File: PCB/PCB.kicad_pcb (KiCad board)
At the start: 2 copper layers, 22.8 x 29.9 mm, 5 parts

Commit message: feat: add components
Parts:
- added U1: STM32G031F6P6, Package_SO:TSSOP-20_4.4x6.5mm_P0.65mm, F.Cu at (157.9, 69.3)
- added U2: XN297L, Package_SO:SSOP-16_3.9x4.9mm_P0.635mm, F.Cu at (165.5, 75.5)
- added U3: HT7333-3.3V, Package_TO_SOT_SMD:SOT-89-3, F.Cu at (165.5, 68.5)
- GND1, SN1, SN2, SN3, VCC1: footprint TestPoint:TestPoint_THTPad_2.0x2.0mm_Drill1.0mm -> TestPoint:TestPoint_THTPad_1.0x1.0mm_Drill0.5mm
- moved GND1 5.41 mm to (155.0, 83.5)
- moved SN3 5.41 mm to (167.0, 83.5)
- moved SN2 4.74 mm to (164.0, 83.5)
- moved VCC1 4.74 mm to (158.0, 83.5)
- moved SN1 4.50 mm to (161.0, 83.5)
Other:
- board size 22.8 x 29.9 mm -> 15 x 20 mm
- board text added: "Nano2A - By Abstractmelon"
- board text removed: "By Abstractmelon"
- board text removed: "Nano2A"

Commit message: feat: added all components
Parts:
- added C1: C, Capacitor_SMD:C_0402_1005Metric, F.Cu at (162.0, 74.0)
- added C2: C, Capacitor_SMD:C_0402_1005Metric, F.Cu at (160.5, 76.0)
- added C3: C, Capacitor_SMD:C_0402_1005Metric, F.Cu at (162.0, 76.0)
- added C4: C, Capacitor_SMD:C_0402_1005Metric, F.Cu at (154.5, 78.0)
- added C5: C, Capacitor_SMD:C_0402_1005Metric, F.Cu at (156.5, 78.0)
- added C6: C, Capacitor_SMD:C_0402_1005Metric, F.Cu at (158.4, 78.0)
- added C7: C, Capacitor_SMD:C_0603_1608Metric, F.Cu at (159.5, 74.0)
- added L1: L, Inductor_SMD:L_0402_1005Metric, F.Cu at (158.9, 76.2)
- added Y1: Crystal, Crystal:Crystal_SMD_3225-4Pin_3.2x2.5mm, F.Cu at (155.9, 74.8)
- moved U2 1.13 mm to (165.5, 74.4)
- moved U3 1.12 mm to (166.0, 67.5)

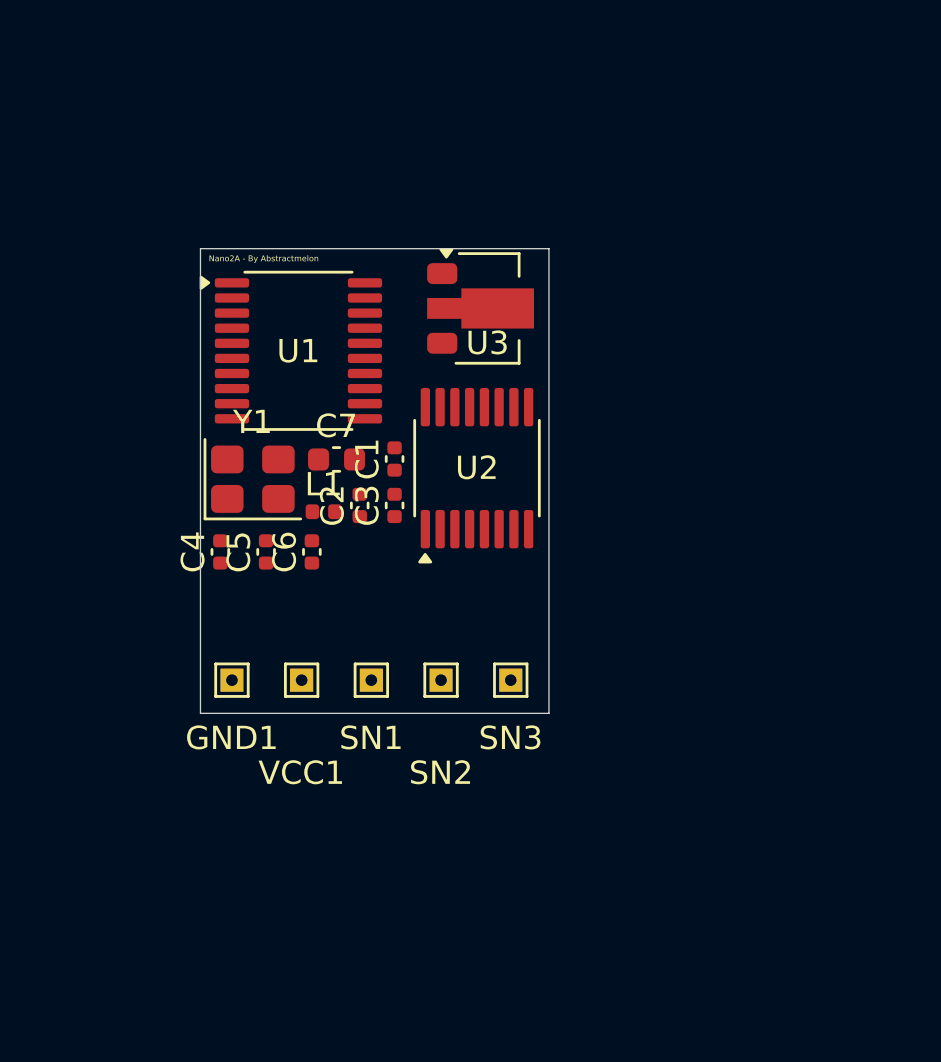
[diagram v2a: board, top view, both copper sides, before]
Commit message: feat: update PCB traces and move components
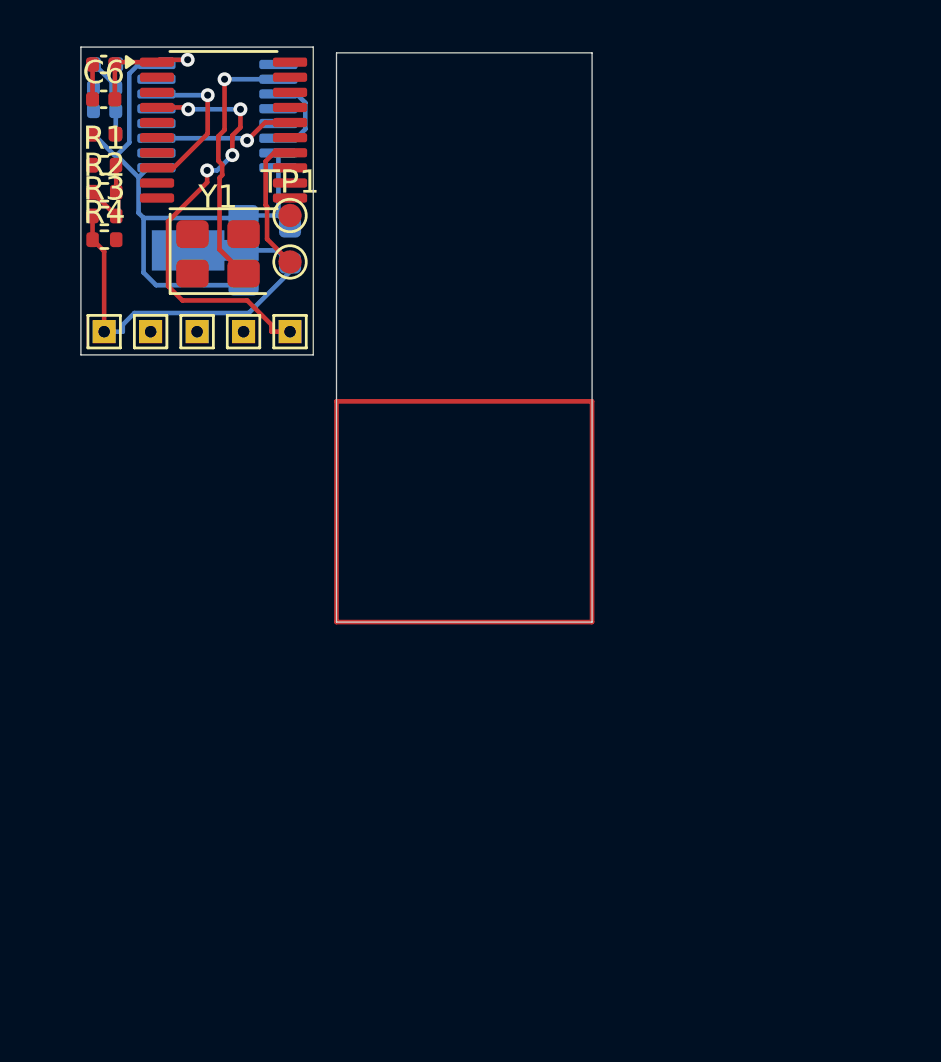
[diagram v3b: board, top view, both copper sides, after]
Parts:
- removed SN1: Channel 1, TestPoint:TestPoint_THTPad_1.0x1.0mm_Drill0.5mm
- removed SN2: Channel 2, TestPoint:TestPoint_THTPad_1.0x1.0mm_Drill0.5mm
- removed SN3: Channel 3, TestPoint:TestPoint_THTPad_1.0x1.0mm_Drill0.5mm
- added CH1: Channel 1, TestPoint:TestPoint_THTPad_1.0x1.0mm_Drill0.5mm, F.Cu at (153.5, 68.5)
- added CH2: Channel 2, TestPoint:TestPoint_THTPad_1.0x1.0mm_Drill0.5mm, F.Cu at (155.5, 68.5)
- added CH3: Channel 3, TestPoint:TestPoint_THTPad_1.0x1.0mm_Drill0.5mm, F.Cu at (157.5, 68.5)
- added R1: R, Resistor_SMD:R_0402_1005Metric, F.Cu at (149.5, 61.3)
- added R2: R, Resistor_SMD:R_0402_1005Metric, F.Cu at (149.5, 62.5)
- added R3: R, Resistor_SMD:R_0402_1005Metric, F.Cu at (149.5, 63.5)
- added R4: R, Resistor_SMD:R_0402_1005Metric, F.Cu at (149.5, 64.5)
- added TP1: SWDIO, TestPoint:TestPoint_Pad_D1.0mm, F.Cu at (157.5, 63.5)
- added TP2: SWCLK, TestPoint:TestPoint_Pad_D1.0mm, F.Cu at (157.5, 65.5)
- C1, C2, C3, C4, C7, U2, U3: moved to B.Cu
- moved C5 22.1 mm to (149.5, 57.0), turned to 0 degrees
- moved C3 21.9 mm to (149.5, 58.0), turned to 180 degrees
- moved C6 21.4 mm to (149.5, 58.5), turned to 0 degrees
- moved C1 21.0 mm to (149.6, 57.0), turned to 0 degrees
- moved C2 20.2 mm to (149.5, 59.0), turned to 180 degrees
- moved U2 18.8 mm to (154.4, 59.2), turned to 0 degrees
- moved L1 18.8 mm to (149.5, 60.0)
- moved C4 18.7 mm to (149.5, 60.0), turned to 180 degrees
- moved VCC1 16.3 mm to (151.5, 68.5), turned to 0 degrees
- moved GND1 16.0 mm to (149.5, 68.5), turned to 0 degrees
- moved U3 12.7 mm to (153.6, 65.0), turned to 180 degrees
- moved U1 10.0 mm to (154.6, 59.8)
- moved Y1 9.82 mm to (154.4, 65.2)
- moved C7 9.44 mm to (157.5, 64.8), turned to 90 degrees
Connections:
- C1 pad 1: unconnected-(C1-Pad1) -> /GND
- C1 pad 2: unconnected-(C1-Pad2) -> /ANT
- C2 pad 1: unconnected-(C2-Pad1) -> /GND
- C2 pad 2: unconnected-(C2-Pad2) -> /XC1
- C3 pad 1: unconnected-(C3-Pad1) -> /GND
- C3 pad 2: unconnected-(C3-Pad2) -> /XC2
- C4 pad 1: unconnected-(C4-Pad1) -> /GND
- C4 pad 2: unconnected-(C4-Pad2) -> /+3.3V
- C5 pad 1: unconnected-(C5-Pad1) -> /GND
- C5 pad 2: unconnected-(C5-Pad2) -> /+3.3V
- C6 pad 1: unconnected-(C6-Pad1) -> /GND
- C6 pad 2: unconnected-(C6-Pad2) -> /+3.3V
- C7 pad 1: unconnected-(C7-Pad1) -> /GND
- C7 pad 2: unconnected-(C7-Pad2) -> /+3.3V
- GND1 pad 1: unconnected-(GND1-Pad1) -> /GND
- L1 pad 2: unconnected-(L1-Pad2) -> /ANT
- U1 pad 1: unconnected-(U1-VDD-Pad1) -> /+3.3V
- U1 pad 14: unconnected-(U1-PA14-Pad14) -> /SWCLK
- U1 pad 15: unconnected-(U1-NRST-Pad15) -> /NRST
- U1 pad 16: unconnected-(U1-PB0-Pad16) -> /CSN
- U1 pad 2: unconnected-(U1-PA0-Pad2) -> /ADC
- U1 pad 3: unconnected-(U1-PA1-Pad3) -> /CH2
- U1 pad 4: unconnected-(U1-PA2-Pad4) -> /CH3
- U1 pad 5: unconnected-(U1-PA3-Pad5) -> /CE
- U1 pad 6: unconnected-(U1-PA4-Pad6) -> /IRQ
- U1 pad 7: unconnected-(U1-PA5-Pad7) -> /SCK
- U1 pad 8: unconnected-(U1-PA6-Pad8) -> /MISO
- U1 pad 9: unconnected-(U1-PA7-Pad9) -> /MOSI
- U2 pad 1: unconnected-(U2-VCC-Pad1) -> /+3.3V
- U2 pad 10: unconnected-(U2-XC2-Pad10) -> /XC2
- U2 pad 11: unconnected-(U2-VSS-Pad11) -> /GND
- U2 pad 12: unconnected-(U2-ANT-Pad12) -> /ANT
- U2 pad 13: unconnected-(U2-IREF-Pad13) -> /IREF
- U2 pad 14: unconnected-(U2-VSS_PA-Pad14) -> /GND
- U2 pad 15: unconnected-(U2-VDD_PA-Pad15) -> /+3.3V
- U2 pad 16: unconnected-(U2-VCC_PA-Pad16) -> /+3.3V
- U2 pad 2: unconnected-(U2-CE-Pad2) -> /CE
- U2 pad 3: unconnected-(U2-CSN-Pad3) -> /CSN
- U2 pad 4: unconnected-(U2-SCK-Pad4) -> /SCK
- U2 pad 5: unconnected-(U2-MOSI-Pad5) -> /MOSI
- U2 pad 6: unconnected-(U2-MISO-Pad6) -> /MISO
- U2 pad 7: unconnected-(U2-IRQ-Pad7) -> /IRQ
- U2 pad 8: unconnected-(U2-VDD-Pad8) -> /+3.3V
- U2 pad 9: unconnected-(U2-XC1-Pad9) -> /XC1
- U3 pad 1: unconnected-(U3-VIN-Pad1) -> /+3.3V
- U3 pad 2: unconnected-(U3-GND-Pad2) -> /GND
- U3 pad 3: unconnected-(U3-VOUT-Pad3) -> /+3.3V
- Y1 pad 1: unconnected-(Y1-Pad1) -> /XC1
- Y1 pad 2: unconnected-(Y1-Pad2) -> /XC2
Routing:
- net /+3.3V: track 0.00 -> 34.0 mm, vias 0 -> 1
- net /GND: track 0.00 -> 25.8 mm
- net /CH3: track 0.00 -> 19.0 mm, vias 0 -> 4
- net /XC2: track 0.00 -> 11.3 mm, vias 0 -> 1
- net /MISO: track 0.00 -> 6.68 mm, vias 0 -> 1
- net /CSN: track 0.00 -> 6.11 mm, vias 0 -> 1
- net /SWCLK: track 0.00 -> 5.97 mm
- net /ADC: track 0.00 -> 1.44 mm
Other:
- board size 15 x 20 mm -> 22 x 24.8 mm
- board text removed: "Nano2A - By Abstractmelon"

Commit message: fix: add component values
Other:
- board size 22 x 24.8 mm -> 10 x 13.2 mm
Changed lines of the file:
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@@
-	)
-	(gr_rect
-		(start 159.5 71.5)
-		(end 170.5 81)
-		(stroke
-			(width 0.2)
-			(type default)
-		)
-		(fill no)
-		(layer "F.Cu")
 	)
 	(gr_rect
@@
 		(stroke
 			(width 0.05)
-			(type solid)
-		)
-		(fill no)
-		(layer "Edge.Cuts")
-	)
-	(gr_rect
-		(start 159.5 56.5)
-		(end 170.5 81)
-		(stroke
-			(width 0.05)

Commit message: feat: add LTSC part numbers
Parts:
- C1: value C -> 2.7pF
- C2, C3: value C -> 22pF
- C4, C5, C6: value C -> 100nF
- C7: value C -> 10µF
- L1: value L -> 2.2nH
- R1, R2: value R -> 10k
- R3: value R -> 1.8k
- R4: value R -> 22k
- U2: value XN297L -> A7106
- Y1: value Crystal -> 16MHz
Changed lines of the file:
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@@
 			(outputformat 1)
 			(mirror no)
-			(drillshape 1)
+			(drillshape 0)
 			(scaleselection 1)
-			(outputdirectory "")
+			(outputdirectory "../output/")
 		)
 	)
@@
 			)
 		)
-		(property "Value" "R"
+		(property "Value" "22k"
 			(at -2.01 1.46 0)
 			(layer "F.Fab")
@@
 			)
 		)
-		(property "Value" "L"
+		(property "Value" "2.2nH"
 			(at 0 1.17 0)
 			(layer "F.Fab")
@@
 			)
 		)
-		(property "Value" "C"
+		(property "Value" "100nF"
 			(at 0 1.16 0)
 			(layer "F.Fab")
@@
 			)
 		)
-		(property "Value" "Crystal"
+		(property "Value" "16MHz"
 			(at 5.1 6.35 0)
 			(layer "F.Fab")
@@
 			)
 		)
-		(property "Value" "C"
+		(property "Value" "100nF"
 			(at 0.065 0.19 0)
 			(layer "F.Fab")
@@
 			)
 		)
-		(property "Value" "R"
+		(property "Value" "10k"
 			(at 0 0.545 0)
 			(layer "F.Fab")
@@
 			)
 		)
-		(property "Value" "R"
+		(property "Value" "1.8k"
 			(at 0 0.2 0)
 			(layer "F.Fab")
@@
 			)
 		)
-		(property "Value" "R"
+		(property "Value" "10k"
 			(at 0 0.2 0)
 			(layer "F.Fab")
@@
 			)
 		)
-		(property "Value" "C"
+		(property "Value" "22pF"
 			(at 0 -0.19 0)
 			(layer "B.Fab")
@@
 			)
 		)
-		(property "Value" "C"
+		(property "Value" "22pF"
 			(at 0 -0.535 0)
 			(layer "B.Fab")
@@
 			)
 		)
-		(property "Value" "XN297L"
+		(property "Value" "A7106"
 			(at 0 -3.4 0)
 			(layer "B.Fab")
@@
 			)
 		)
-		(property "Value" "C"
+		(property "Value" "10µF"
 			(at 0 -1.43 90)
 			(layer "B.Fab")
@@
 			)
 		)
-		(property "Value" "C"
+		(property "Value" "2.7pF"
 			(at 0 -1.16 0)
 			(layer "B.Fab")
@@
 			)
 		)
-		(property "Value" "C"
+		(property "Value" "100nF"
 			(at 0 -0.19 0)
 			(layer "B.Fab")

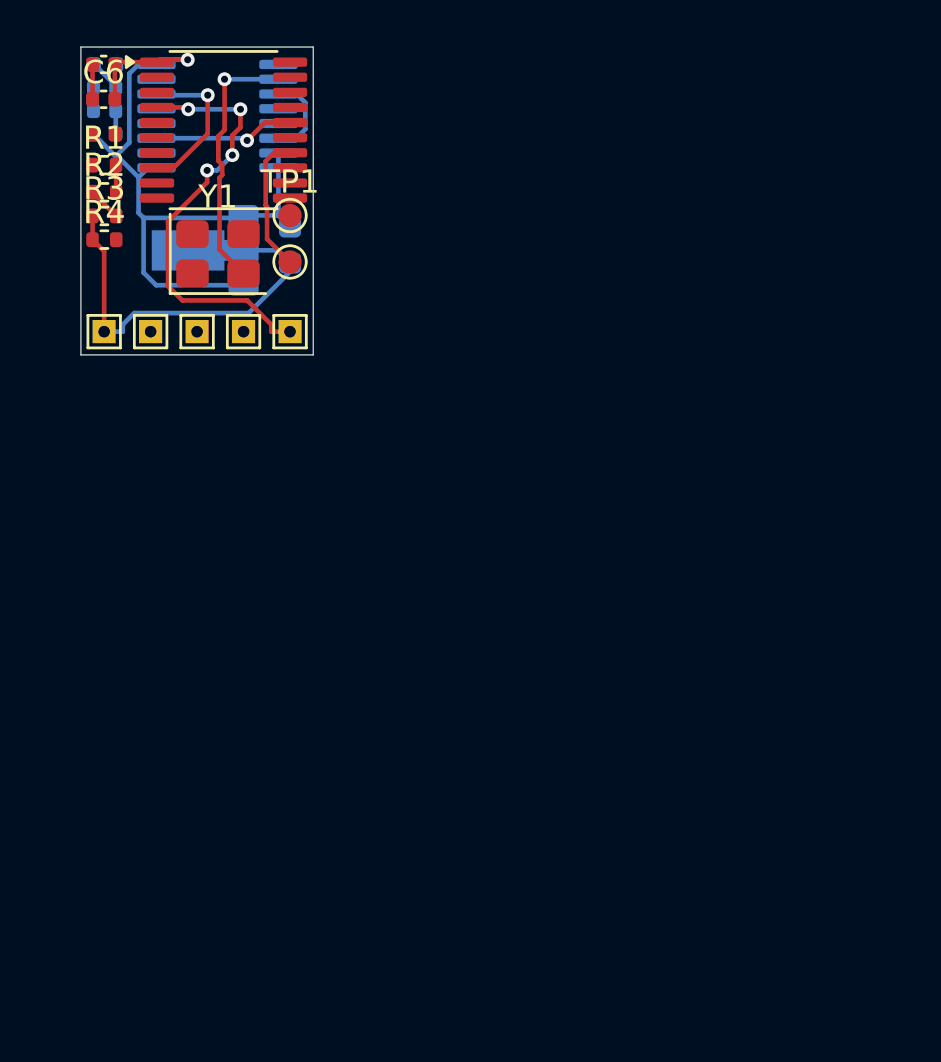
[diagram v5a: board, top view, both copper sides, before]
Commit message: feat: update PCB from schematic
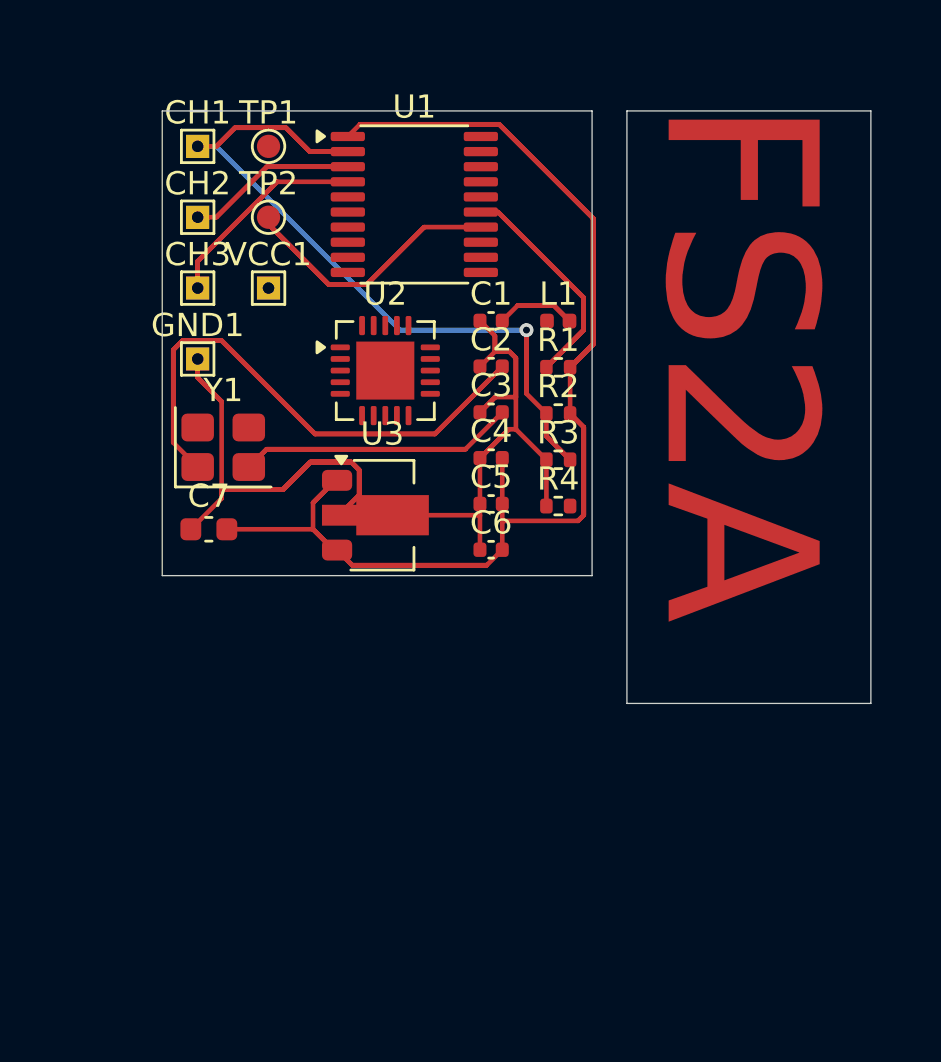
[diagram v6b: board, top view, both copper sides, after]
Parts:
- C1, C2, C3, C4, C7, U3: moved to F.Cu
- U2: footprint Package_SO:SSOP-16_3.9x4.9mm_P0.635mm -> Package_DFN_QFN:QFN-20-1EP_4x4mm_P0.5mm_EP2.5x2.5mm; moved to F.Cu
- moved C6 25.6 mm to (166.2, 77.9)
- moved C5 25.2 mm to (166.2, 75.9)
- moved R4 22.7 mm to (169.0, 76.0)
- moved R3 22.2 mm to (169.0, 74.0)
- moved R2 21.7 mm to (169.0, 72.0)
- moved C3 21.7 mm to (166.2, 72.0), turned to 0 degrees
- moved C4 21.7 mm to (166.2, 73.9), turned to 0 degrees
- moved R1 21.4 mm to (169.0, 70.0)
- moved L1 21.1 mm to (169.0, 68.0)
- moved C2 19.9 mm to (166.2, 70.0), turned to 0 degrees
- moved C1 19.9 mm to (166.2, 68.0)
- moved U3 13.9 mm to (161.5, 76.4), turned to 0 degrees
- moved U2 13.1 mm to (161.6, 70.2)
- moved C7 12.7 mm to (154.0, 77.0), turned to 0 degrees
- moved U1 8.81 mm to (162.8, 63.0)
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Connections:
- U2 pad 1: /+3.3V -> unconnected-(U2-RSSI-Pad1)
- U2 pad 10: /XC2 -> unconnected-(U2-VDA3-Pad10)
- U2 pad 11: /GND -> unconnected-(U2-SCS-Pad11)
- U2 pad 12: /ANT -> unconnected-(U2-SCK-Pad12)
- U2 pad 13: /IREF -> unconnected-(U2-DVDD-Pad13)
- U2 pad 14: /GND -> unconnected-(U2-SDIO-Pad14)
- U2 pad 15: /+3.3V -> unconnected-(U2-GND-Pad15)
- U2 pad 16: /+3.3V -> unconnected-(U2-GIO1-Pad16)
- U2 pad 2: /CE -> unconnected-(U2-BPBG-Pad2)
- U2 pad 3: /CSN -> unconnected-(U2-RFI-Pad3)
- U2 pad 4: /SCK -> unconnected-(U2-RFO-Pad4)
- U2 pad 5: /MOSI -> unconnected-(U2-VDA2-Pad5)
- U2 pad 6: /MISO -> unconnected-(U2-VT-Pad6)
- U2 pad 7: /IRQ -> unconnected-(U2-GND-Pad7)
- U2 pad 8: /+3.3V -> unconnected-(U2-XI-Pad8)
- U2 pad 9: /XC1 -> unconnected-(U2-XO-Pad9)
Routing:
- net /+3.3V: track 34.0 -> 102.5 mm, vias 1 -> 0
- net /GND: track 25.8 -> 85.7 mm
- net /ADC: track 1.44 -> 58.2 mm, vias 0 -> 1
- net /XC1: track 0.00 -> 43.9 mm
- net /SWCLK: track 5.97 -> 30.5 mm
- net /NRST: track 0.00 -> 24.4 mm
- net /CH2: track 0.00 -> 13.9 mm
- net /XC2: track 11.3 -> 21.5 mm, vias 1 -> 0
- net /MISO: track 6.68 -> 0.00 mm, vias 1 -> 0
- net /CSN: track 6.11 -> 0.00 mm, vias 1 -> 0
- net /ANT: track 0.00 -> 5.96 mm
- net /CH3: track 19.0 -> 16.2 mm, vias 4 -> 0
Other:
- board size 10 x 13.2 mm -> 30.5 x 25.5 mm
- board text added: "FS2A"

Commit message: fix: Migrate symbol
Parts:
- moved C1 0.50 mm to (165.7, 68.0)
- moved C2 0.50 mm to (165.7, 70.0)
- moved C3 0.50 mm to (165.7, 72.0)
- moved C4 0.50 mm to (165.7, 73.9)
- moved C5 0.50 mm to (165.7, 75.9)
- moved C6 0.50 mm to (165.7, 77.9)
- moved C7 0.50 mm to (153.5, 77.0)
- moved CH1 0.50 mm to (153.0, 60.5)
- moved CH2 0.50 mm to (153.0, 63.6)
- moved CH3 0.50 mm to (153.0, 66.6)
- moved GND1 0.50 mm to (153.0, 69.7)
- moved L1 0.50 mm to (168.5, 68.0)
- moved R1 0.50 mm to (168.5, 70.0)
- moved R2 0.50 mm to (168.5, 72.0)
- moved R3 0.50 mm to (168.5, 74.0)
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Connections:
- C7 pad 2: /+3.3V -> /VCC1
- CH1 pad 1: /ADC -> /CH1
- GND1 pad 1: /GND -> Net-(U3-GND)
- R2 pad 2: /+3.3V -> /VCC1
- U1 pad 1: /+3.3V -> Net-(U1-VDD)
- U1 pad 14: /SWCLK -> unconnected-(U1-PA14-Pad14)
- U1 pad 15: /NRST -> unconnected-(U1-NRST-Pad15)
- U1 pad 16: /CSN -> unconnected-(U1-PB0-Pad16)
- U1 pad 2: /ADC -> unconnected-(U1-PA0-Pad2)
- U1 pad 3: /CH2 -> unconnected-(U1-PA1-Pad3)
- U1 pad 4: /CH3 -> unconnected-(U1-PA2-Pad4)
- U1 pad 5: /CE -> unconnected-(U1-PA3-Pad5)
- U1 pad 6: /IRQ -> unconnected-(U1-PA4-Pad6)
- U1 pad 7: /SCK -> unconnected-(U1-PA5-Pad7)
- U1 pad 8: /MISO -> unconnected-(U1-PA6-Pad8)
- U1 pad 9: /MOSI -> unconnected-(U1-PA7-Pad9)
- U3 pad 1: /+3.3V -> Net-(U3-VIN)
- U3 pad 2: /GND -> Net-(U3-GND)
- U3 pad 3: /+3.3V -> Net-(U1-VDD)
- VCC1 pad 1: unconnected-(VCC1-Pad1) -> Net-(U3-VIN)
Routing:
- net /+3.3V: track 102.5 -> 0.00 mm
- net /GND: track 85.7 -> 0.00 mm
- net /ADC: track 58.2 -> 0.00 mm, vias 1 -> 0
- net /XC1: track 43.9 -> 0.00 mm
- net /SWCLK: track 30.5 -> 0.00 mm
- net /NRST: track 24.4 -> 0.00 mm
- net /XC2: track 21.5 -> 0.00 mm
- net /CH3: track 16.2 -> 0.00 mm
- net /CH2: track 13.9 -> 0.00 mm
- net /ANT: track 5.96 -> 0.00 mm
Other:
- board size 30.5 x 25.5 mm -> 31 x 25.5 mm
